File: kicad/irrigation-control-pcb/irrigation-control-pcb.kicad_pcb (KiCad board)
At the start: 2 copper layers, 67 x 67 mm, 18 parts, among them P1 x, P2 x

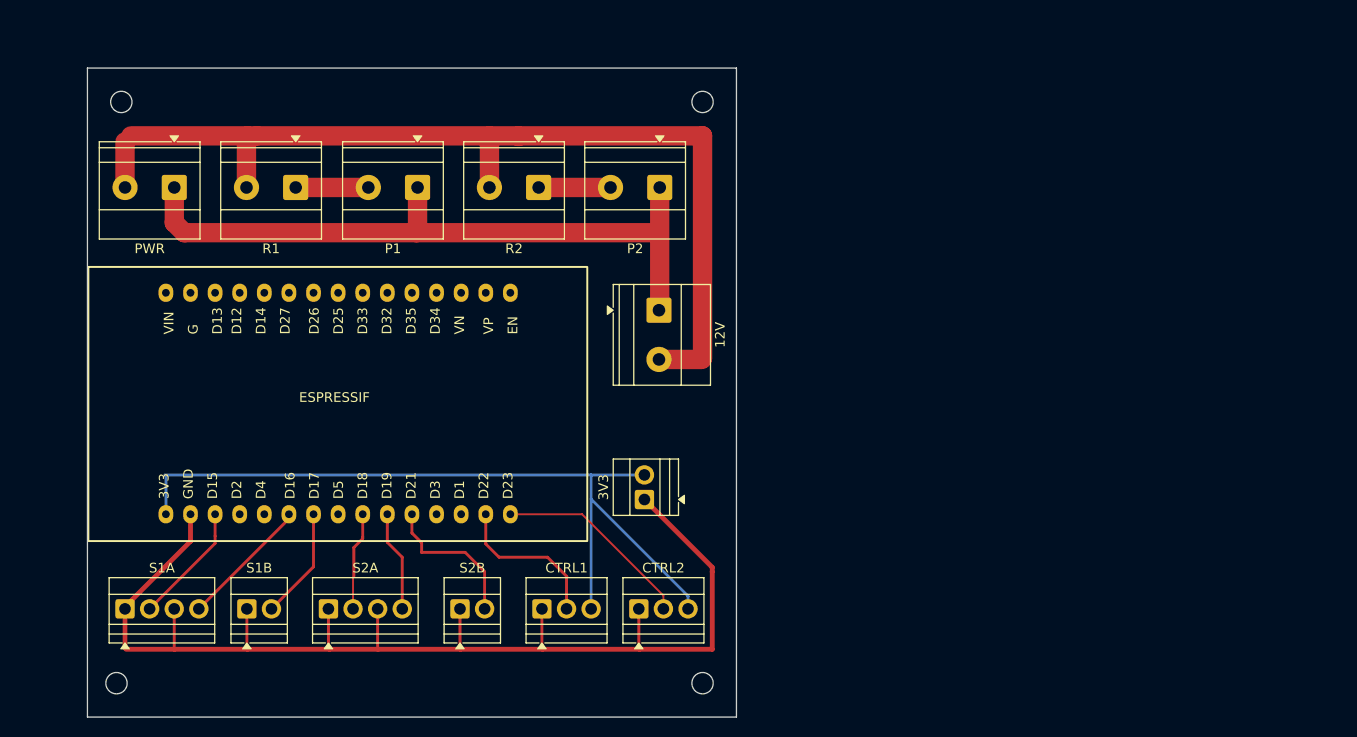
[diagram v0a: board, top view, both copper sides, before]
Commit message: added switch terminal
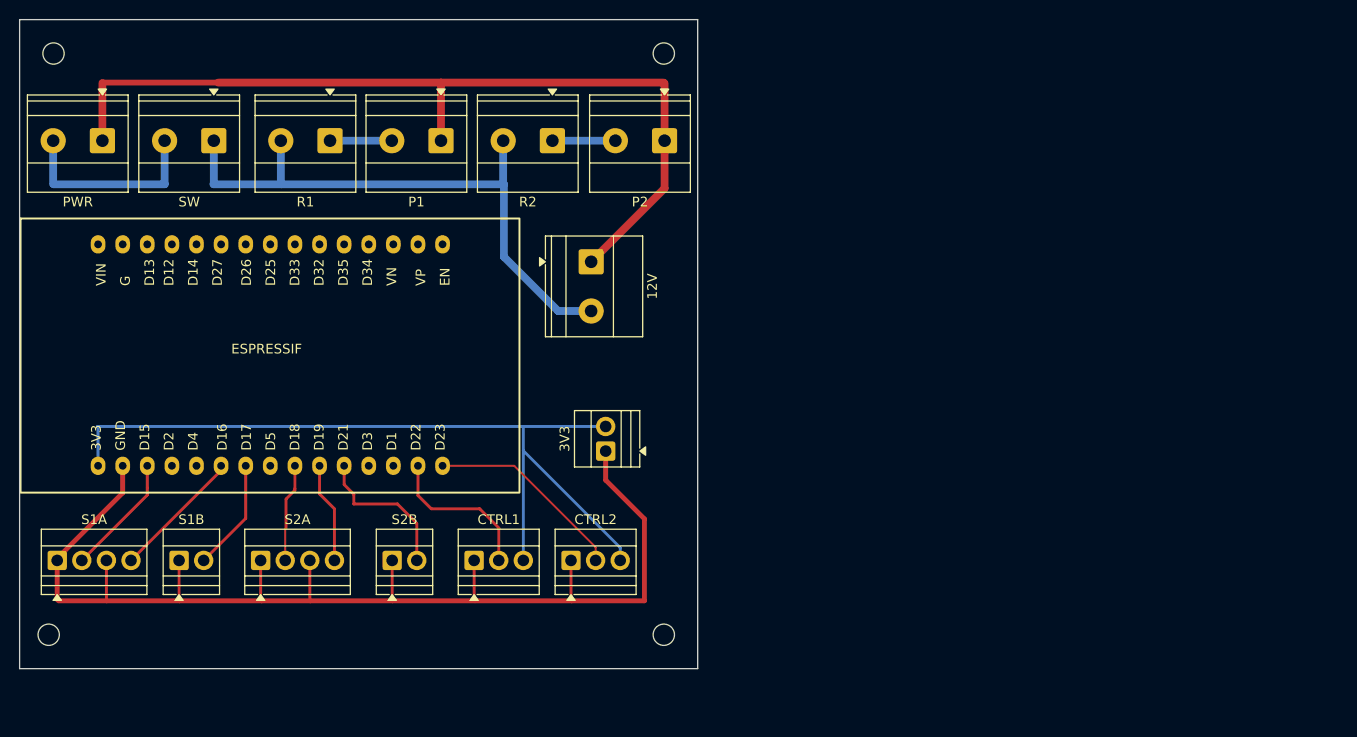
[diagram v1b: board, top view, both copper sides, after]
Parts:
- added SW: x, TerminalBlock_Phoenix:TerminalBlock_Phoenix_MKDS-1,5-2-5.08_1x02_P5.08mm_Horizontal, F.Cu at (70.0, 62.5)
- moved PWR 8.85 mm to (58.5, 62.5)
- moved 12V 8.60 mm to (109.0, 75.0)
- moved CTRL1 8.60 mm to (96.9, 105.8)
- moved CTRL2 8.60 mm to (106.9, 105.8)
- moved ESPRESSIF 8.60 mm to (75.5, 84.5)
- moved S1A 8.60 mm to (53.9, 105.8)
- moved S1B 8.60 mm to (66.5, 105.8)
- moved S2A 8.60 mm to (74.9, 105.8)
- moved S2B 8.60 mm to (88.5, 105.8)
- moved hole1 8.60 mm to (53.5, 53.5)
- moved hole1 8.60 mm to (53.0, 113.5)
- moved 3V3 6.40 mm to (110.5, 94.5)
- moved hole1 6.40 mm to (116.5, 53.5)
- moved hole1 6.40 mm to (116.5, 113.5)
- moved R1 5.99 mm to (82.0, 62.5)
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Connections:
- 12V pad 1: (no net) -> Power
- 12V pad 2: (no net) -> Power
- P1 pad 1: (no net) -> Power
- P1 pad 2: (no net) -> Power
- P2 pad 1: (no net) -> Power
- P2 pad 2: (no net) -> Power
- PWR pad 1: (no net) -> Power
- PWR pad 2: (no net) -> Power
- R1 pad 1: (no net) -> Power
- R1 pad 2: (no net) -> Power
- R2 pad 1: (no net) -> Power
- R2 pad 2: (no net) -> Power
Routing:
- net Power: track 0.00 -> 189.1 mm
- net (no net): track 506.9 -> 320.9 mm
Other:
- board size 67 x 67 mm -> 70 x 67 mm

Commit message: improved esp32 footprint
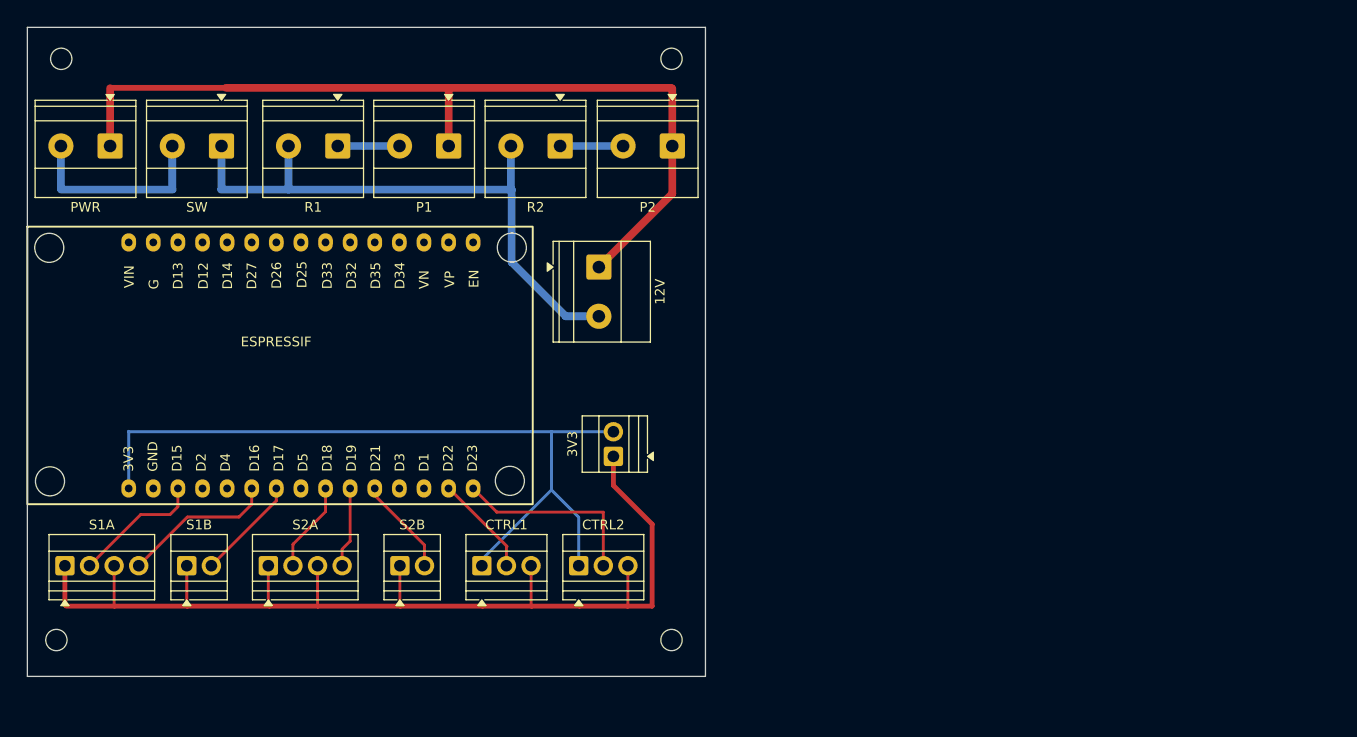
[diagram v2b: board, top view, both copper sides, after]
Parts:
- removed the ESPRESSIF at (75.5, 84.5)
- added ESPRESSIF: ESP_Test, AA_Maker_Space:ESP-32-WROOM-32, F.Cu at (50.8, 71.4)
- moved 12V 0.97 mm to (109.8, 75.5)
- moved S1B 0.97 mm to (67.3, 106.4)
- moved S2A 0.97 mm to (75.7, 106.4)
- moved S2B 0.97 mm to (89.3, 106.4)
- moved hole1 0.97 mm to (117.3, 114.0)
- moved P1 0.97 mm to (94.3, 63.0)
- moved P2 0.97 mm to (117.4, 63.0)
- moved R2 0.97 mm to (105.8, 63.0)
- moved hole1 0.97 mm to (117.3, 54.0)
- moved S1A 0.97 mm to (54.7, 106.4)
- moved hole1 0.97 mm to (53.8, 114.0)
- moved 3V3 0.97 mm to (111.3, 95.1)
- moved PWR 0.97 mm to (59.3, 63.0)
- moved hole1 0.97 mm to (54.3, 54.0)
- moved CTRL1 0.97 mm to (97.7, 106.4)
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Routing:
- net (no net): track 320.9 -> 292.3 mm

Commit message: add some text about normalizing holes
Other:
- board text added: "TODO: - normalize where holes are - allow m3 for holes - group relay with sensors - labels on outside - reduce space inside sensor terminals"
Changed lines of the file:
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@@
 		(layer "Edge.Cuts")
+	)
+	(gr_text "TODO:\n- normalize where holes are\n- allow m3 for holes\n- group relay with sensors\n- labels on outside\n- reduce space inside sensor terminals"
+		(at 130.302 82.55 0)
+		(layer "F.Cu")
+		(effects
+			(font
+				(size 1.5 1.5)
+				(thickness 0.3)
+				(bold yes)
+			)
+			(justify left bottom)
+		)
 	)
 	(segment
